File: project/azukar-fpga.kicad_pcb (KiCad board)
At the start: 2 copper layers, 100 x 75 mm, 168 parts, among them J1 USB_C_Receptacle_USB2.0_16P, P1 Conector 2x10, P2 Conector 2x10, P3 Conector 2x10, P4 Conector 2x10, SW1 SW_Push, SW2 SW_Push, SW3 SW_Push, SW4 SW_Push, SW5 SW_Push, SW6 SW_Push, SW7 SW_Push, SW8 SW_Push, U1 LD1117S33CTR, U2 LD1117S12CTR, U3 USBLC6-2SC6, U4 FT2232HL, U5 M93C66, U6 ICE40HX4K-TQ144, U7 W25X40CLSN, Y1 ECS-3225MV-120-CN-TR, Y2 ECS-3225MVQ-1000-CN-TR

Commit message: Mejoras en pcb
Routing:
- net /Memorias y PLL/Flash_DI: track 35.0 -> 28.7 mm
- net /Memorias y PLL/Flash_DO: track 35.6 -> 33.6 mm
- net GND: track 443.4 -> 444.6 mm
- net /Perifericos/LED8: track 43.5 -> 44.6 mm
- net /Perifericos/VUART_Tx: track 17.3 -> 18.4 mm
- net /Memorias y PLL/Flash_RESET: track 22.8 -> 23.8 mm
- net /Memorias y PLL/Flash_SCK: track 43.1 -> 44.0 mm
- net /Perifericos/VUART_CTS: track 15.8 -> 16.3 mm
- net /Perifericos/VUART_Rx: track 15.4 -> 15.9 mm

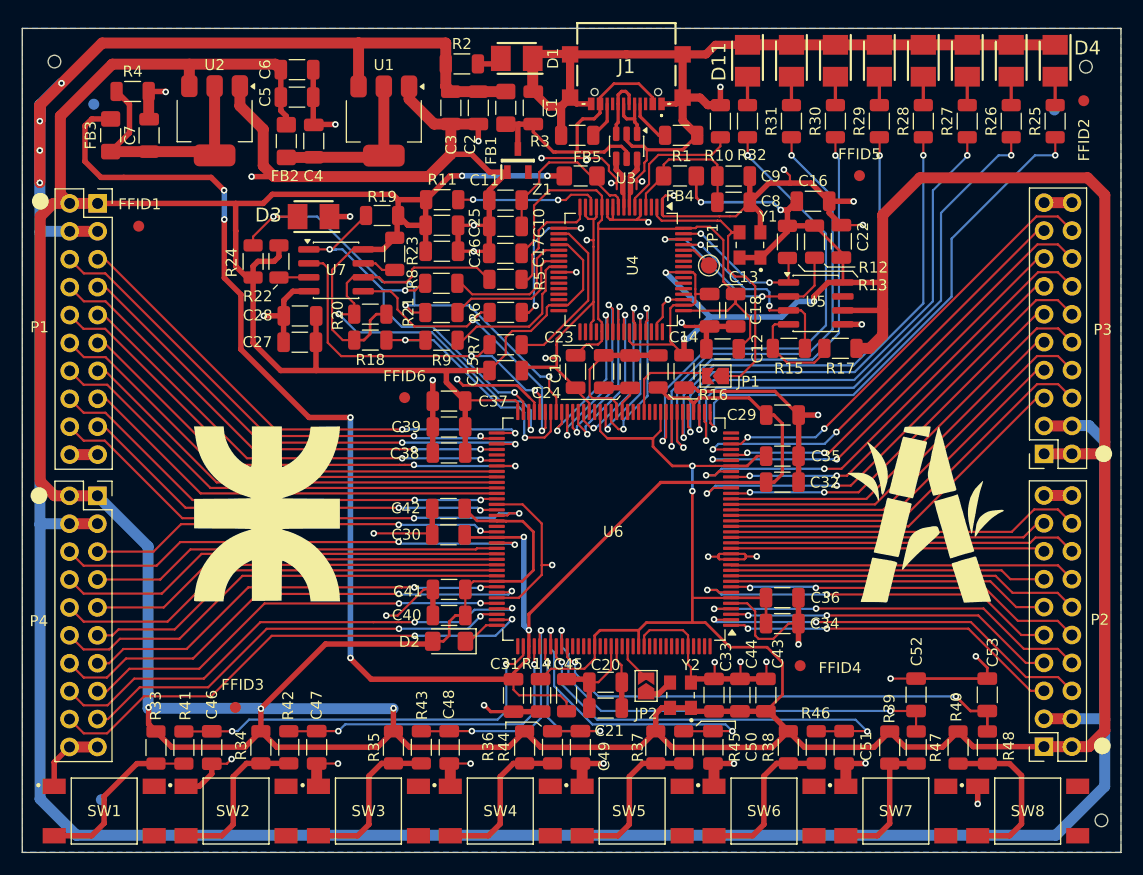
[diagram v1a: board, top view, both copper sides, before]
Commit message: Corregidos footprints, generada nuevas capturas, cambiado regulador por TLV761
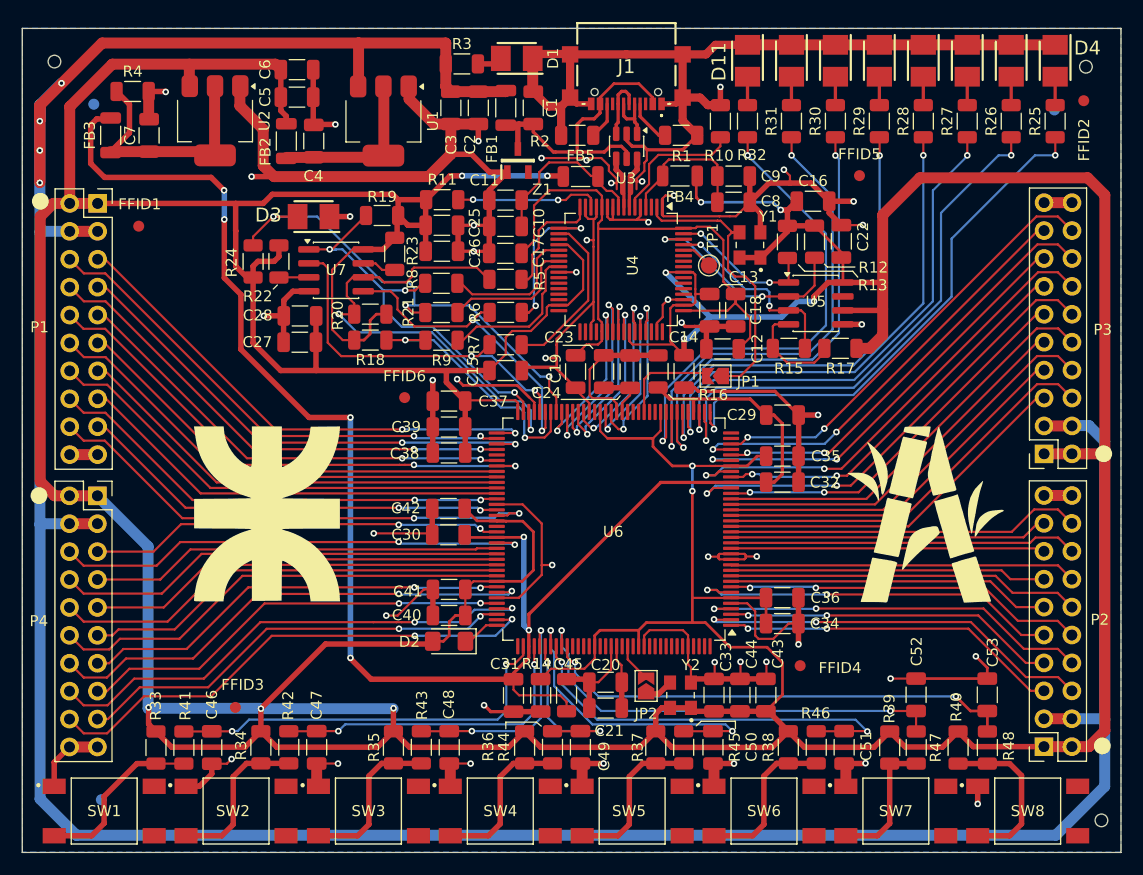
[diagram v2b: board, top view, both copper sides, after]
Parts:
- FB1, FB2, FB3, FB4, FB5: footprint Inductor_SMD:L_1206_3216Metric_Pad1.42x1.75mm_HandSolder -> Inductor_SMD:L_1206_3216Metric
- U1: value LD1117S33CTR -> TLV76133DCYR
- U2: value LD1117S12CTR -> TLV76112DCYR
- renumbered R3 to R2, R2 to R3
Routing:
- net +1V2: track 159.4 -> 158.5 mm
- net +3V3: track 678.6 -> 677.8 mm
- net /USB-FTDI/VPLL: track 15.7 -> 16.4 mm
